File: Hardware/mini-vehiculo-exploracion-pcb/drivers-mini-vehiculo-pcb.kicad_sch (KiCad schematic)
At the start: 25 parts, among them J1 Conn_01x08_Pin_drv, J2 Conn_01x02_Pin, J3 Conn_01x02_Motor1, J4 Conn_01x02_Motor2, J5 Conn_01x02_Servo, U3 DRV8873HPWPRQ1, U4 DRV8873HPWPRQ1

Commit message: updated pcb drv
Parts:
- removed J5: Conn_01x02_Servo, symbol Connector:Conn_01x02_Pin
- added J3: Conn_01x03_Pin, symbol Connector:Conn_01x03_Pin
- C1: renamed from C9; value 1000u -> 180u; footprint (none) -> EMZR160ARA221MF61G:CAPAE660X610N
- C7: renamed from C10; value 1000u -> 180u; footprint (none) -> EMZR160ARA221MF61G:CAPAE660X610N
- J1: footprint (none) -> JST_Connectors:JST_8PIN
- renumbered C12 to C10, C4 to C11, C13 to C12, C1 to C2, C6 to C3, C7 to C4, C3 to C5, C8 to C6, C2 to C8, C11 to C9, J3 to J4, J4 to J5, R2 to R1, R5 to R2, R1 to R3, R3 to R4, R6 to R5, R4 to R6, U3 to U1, U4 to U2
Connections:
- net +5V: now also J3.1 (Pin_1)
- net GND: now also J3.3 (Pin_3)
- net CTRL_SERVO renamed SERVO_CRL
- net SERVO_CRL: now also J3.2 (Pin_2)
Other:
- added sheet Battery Sensor (battery_sensor.kicad_sch)
- note added: "IO39"
- note added: "TO SERVOMOTOR"
- note removed: "POWER SERVOMOTOR"

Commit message: cambios
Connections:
- no-connect marks 2 -> 4
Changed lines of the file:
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@@
 	)
 	(junction
+		(at 74.93 39.37)
+		(diameter 0)
+		(color 0 0 0 0)
+	)
+	(junction
 		(at 184.15 45.72)
 		(diameter 0)
@@
 	)
 	(no_connect
+		(at 74.93 102.87)
+	)
+	(no_connect
 		(at 110.49 97.79)
 	)
@@
 		(at 222.25 99.06)
 	)
+	(no_connect
+		(at 186.69 104.14)
+	)
 	(wire
 		(pts
@@
 					(unit 1)
 				)
+			)
+		)
+	)
+	(symbol
+		(lib_id "power:PWR_FLAG")
+		(at 74.93 39.37 270)
+		(unit 1)
+		(exclude_from_sim no)
+		(in_bom yes)
+		(on_board yes)
+		(dnp no)
+		(fields_autoplaced yes)
+		(property "Reference" "#FLG03"
+			(at 76.835 39.37 0)
+			(effects
+				(font
+					(size 1.27 1.27)
+				)
+				(hide yes)
+			)
+		)
+		(property "Value" "PWR_FLAG"
+			(at 78.74 39.3699 90)
+			(effects
+				(font
+					(size 1.27 1.27)
+				)
+				(justify left)
+			)
+		)
+		(property "Footprint" ""
+			(at 74.93 39.37 0)
+			(effects
+				(font
+					(size 1.27 1.27)
+				)
+				(hide yes)
+			)
+		)
+		(property "Datasheet" "~"
+			(at 74.93 39.37 0)
+			(effects
+				(font
+					(size 1.27 1.27)
+				)
+				(hide yes)
+			)
+		)
+		(property "Description" "Special symbol for telling ERC where power comes from"
+			(at 74.93 39.37 0)
+			(effects
+				(font
+					(size 1.27 1.27)
+				)
+				(hide yes)
+			)
+		)
+		(pin "1"
+		)
+		(instances
+			(project ""
+				(path "/7776e3ee-622a-4a3e-a213-279f6f5df2cb"
+					(reference "#FLG03")
+					(unit 1)
+				)

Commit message: changes etc
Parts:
- C10, C11, C2, C3, C4, C5, C8, C9: footprint capacitores_driver:CAPC2012X88N -> Capacitor_SMD:C_0805_2012Metric_Pad1.18x1.45mm_HandSolder
- C12, C6: footprint capacitores_driver:CAPC2012X140N -> Capacitor_SMD:C_0805_2012Metric_Pad1.18x1.45mm_HandSolder
- J1: footprint JST_Connectors:JST_8PIN -> Connector_PinSocket_2.54mm:PinSocket_1x08_P2.54mm_Vertical
- J2, J4, J5: footprint (none) -> Connector_PinSocket_2.54mm:PinSocket_1x02_P2.54mm_Vertical
- J3: footprint (none) -> Connector_PinSocket_2.54mm:PinSocket_1x03_P2.54mm_Vertical
- U1, U2: footprint DRV8873HPWPRQ1:DRV8873HPWPRQ1 -> DRV8873HPWPRQ1:SOP65P640X120-25N

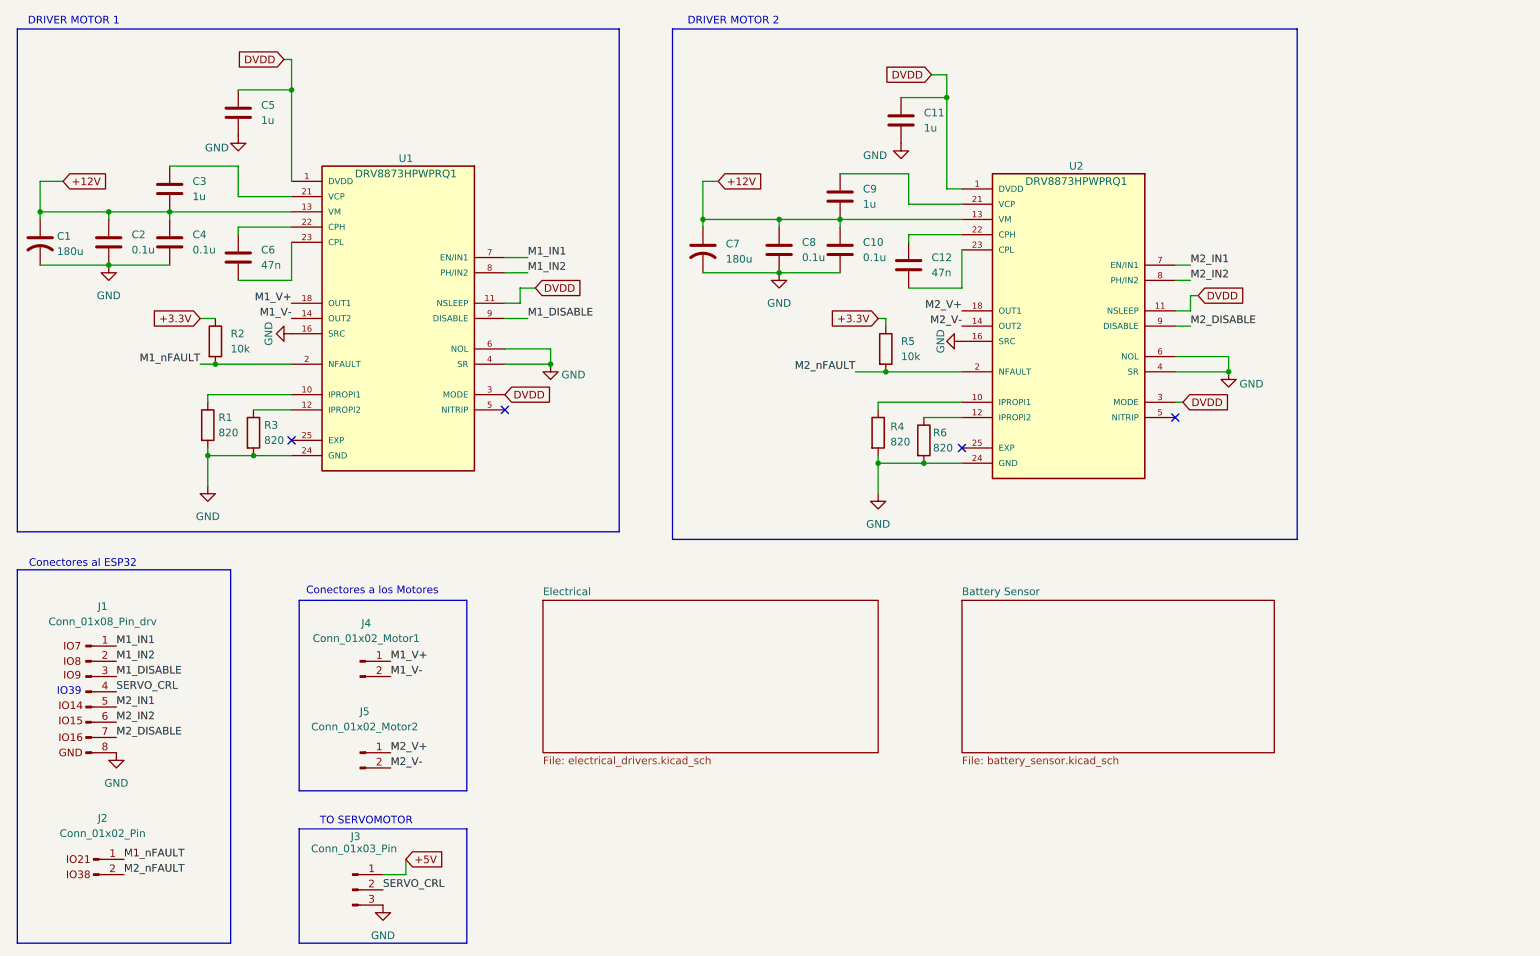
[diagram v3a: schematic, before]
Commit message: updated sockets drv
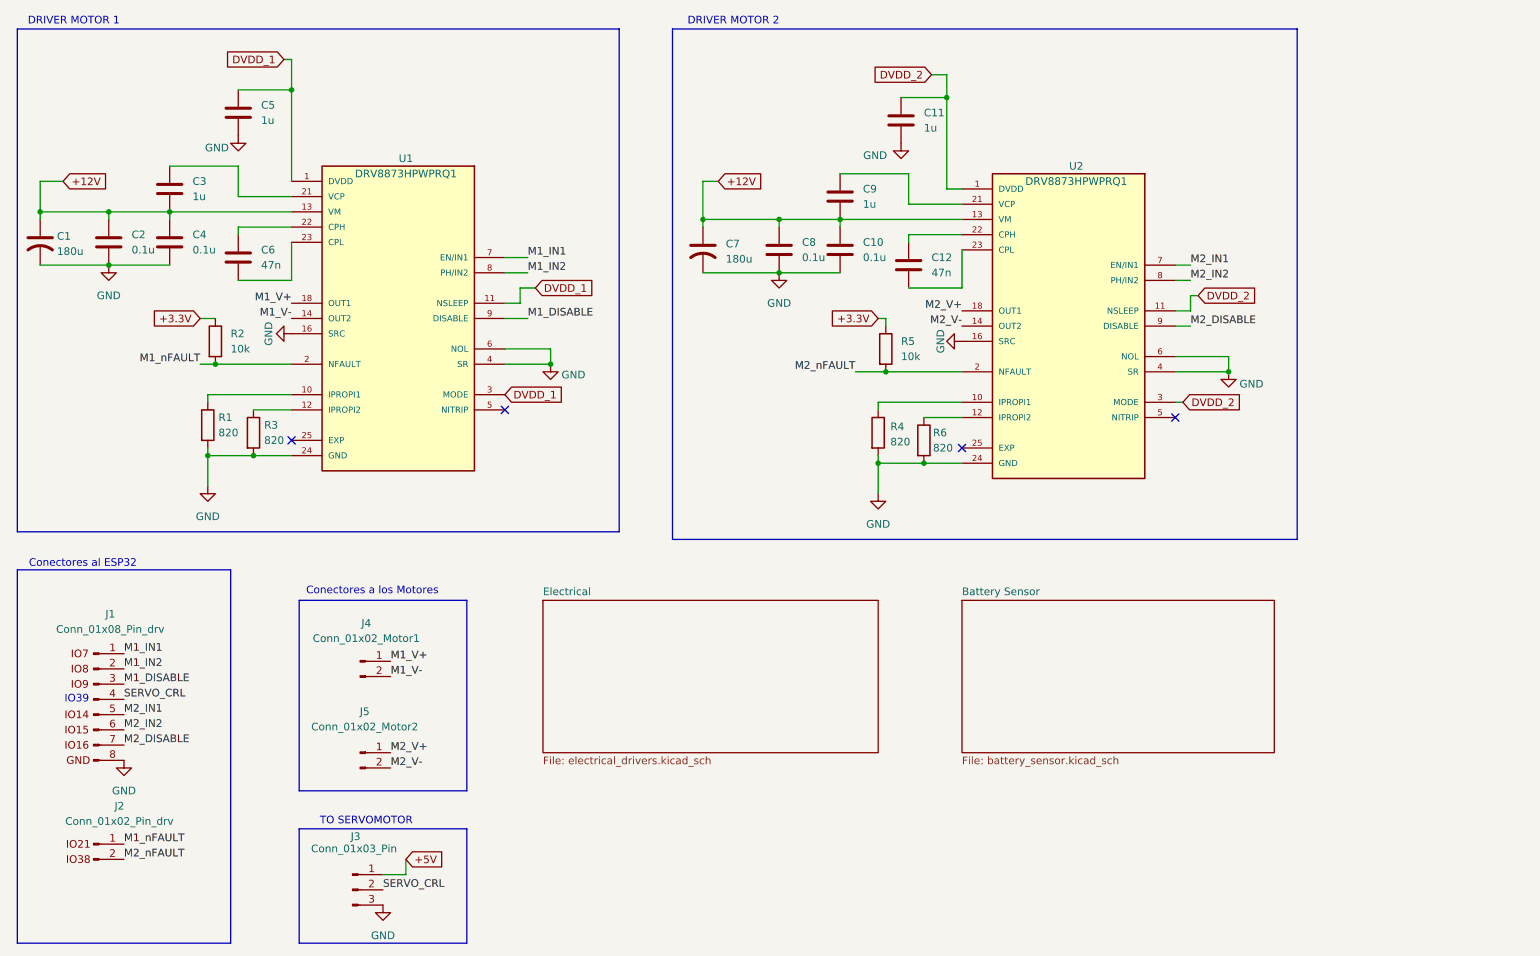
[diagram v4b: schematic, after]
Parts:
- removed J2: Conn_01x02_Pin, Connector_PinSocket_2.54mm:PinSocket_1x02_P2.54mm_Vertical, symbol Connector:Conn_01x02_Pin
- added J2: Conn_01x02_Pin_drv, symbol ConectorDriverESP:Conn_01x02_Pin_drv
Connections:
- net M1_nFAULT: now also J2.1 (Pin_1)
- net M2_nFAULT: now also J2.2 (Pin_2)
- net DVDD renamed DVDD_1
- net DVDD_1: no longer C11.1, U2.1 (DVDD), U2.11 (NSLEEP), U2.3 (MODE)
- new net DVDD_2: C11.1, U2.1 (DVDD), U2.11 (NSLEEP), U2.3 (MODE)
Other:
- moved on the sheet: J1
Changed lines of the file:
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@@
 	(text "IO39"
 		(exclude_from_sim no)
-		(at 37.846 144.78 0)
+		(at 39.116 146.05 0)
 		(effects
 			(font
@@
 	)
 	(label "M2_IN2"
-		(at 45.72 149.86 0)
+		(at 46.99 151.13 0)
 		(effects
 			(font
@@
 	)
 	(label "M1_IN2"
-		(at 45.72 139.7 0)
+		(at 46.99 140.97 0)
 		(effects
 			(font
@@
 	)
 	(label "M2_IN1"
-		(at 45.72 147.32 0)
+		(at 46.99 148.59 0)
 		(effects
 			(font
@@
 	)
 	(label "M1_IN1"
-		(at 45.72 137.16 0)
+		(at 46.99 138.43 0)
 		(effects
 			(font
@@
 	)
 	(label "SERVO_CRL"
-		(at 45.72 144.78 0)
+		(at 46.99 146.05 0)
 		(effects
 			(font
@@
 	)
 	(label "M1_DISABLE"
-		(at 45.72 142.24 0)
+		(at 46.99 143.51 0)
 		(effects
 			(font
@@
 	)
 	(label "M1_nFAULT"
-		(at 46.99 172.72 0)
+		(at 46.99 170.18 0)
 		(effects
 			(font
@@
 	)
 	(label "M2_DISABLE"
-		(at 45.72 152.4 0)
+		(at 46.99 153.67 0)
 		(effects
 			(font
@@
 	)
 	(label "M2_nFAULT"
-		(at 46.99 175.26 0)
+		(at 46.99 172.72 0)
 		(effects
 			(font
@@
 		)
 	)
-	(global_label "DVDD"
+	(global_label "DVDD_1"
 		(shape input)
 		(at 115.57 77.47 0)
@@
 		)
 		(property "Intersheetrefs" "${INTERSHEET_REFS}"
-			(at 123.4538 77.47 0)
+			(at 125.6309 77.47 0)
 			(effects
 				(font
@@
 		)
 	)
-	(global_label "DVDD"
+	(global_label "DVDD_2"
 		(shape input)
 		(at 226.06 78.74 0)
@@
 		)
 		(property "Intersheetrefs" "${INTERSHEET_REFS}"
-			(at 233.9438 78.74 0)
+			(at 236.1209 78.74 0)
 			(effects
 				(font
@@
 		)
 	)
-	(global_label "DVDD"
+	(global_label "DVDD_2"
 		(shape input)
 		(at 181.61 41.91 180)
@@
 		)
 		(property "Intersheetrefs" "${INTERSHEET_REFS}"
-			(at 173.7262 41.91 0)
+			(at 171.5491 41.91 0)
 			(effects
 				(font
@@
 		)
 	)
-	(global_label "DVDD"
+	(global_label "DVDD_1"
 		(shape input)
 		(at 73.66 39.37 180)
@@
 		)
 		(property "Intersheetrefs" "${INTERSHEET_REFS}"
-			(at 65.7762 39.37 0)
+			(at 63.5991 39.37 0)
 			(effects
 				(font
@@
 		)
 	)
-	(global_label "DVDD"
+	(global_label "DVDD_1"
 		(shape input)
 		(at 110.49 95.25 0)
@@
 		)
 		(property "Intersheetrefs" "${INTERSHEET_REFS}"
-			(at 118.3738 95.25 0)
+			(at 120.5509 95.25 0)
 			(effects
 				(font
@@
 		)
 	)
-	(global_label "DVDD"
+	(global_label "DVDD_2"
 		(shape input)
 		(at 223.52 96.52 0)
@@
 		)
 		(property "Intersheetrefs" "${INTERSHEET_REFS}"
-			(at 231.4038 96.52 0)
+			(at 233.5809 96.52 0)
 			(effects
 				(font
@@
 	)
 	(symbol
+		(lib_id "ConectorDriverESP:Conn_01x02_Pin_drv")
+		(at 41.91 170.18 0)
+		(unit 1)
+		(exclude_from_sim no)
+		(in_bom yes)
+		(on_board yes)
+		(dnp no)
+		(property "Reference" "J2"
+			(at 46.228 163.83 0)
+			(effects
+				(font
+					(size 1.27 1.27)
+				)
+			)
+		)
+		(property "Value" "Conn_01x02_Pin_drv"
+			(at 46.228 166.37 0)
+			(effects
+				(font
+					(size 1.27 1.27)
+				)
+			)
+		)
+		(property "Footprint" ""
+			(at 41.91 170.18 0)
+			(effects
+				(font
+					(size 1.27 1.27)
+				)
+				(hide yes)
+			)
+		)
+		(property "Datasheet" "~"
+			(at 41.91 170.18 0)
+			(effects
+				(font
+					(size 1.27 1.27)
+				)
+				(hide yes)
+			)
+		)
+		(property "Description" "Generic connector, single row, 01x02, script generated"
+			(at 41.91 170.18 0)
+			(effects
+				(font
+					(size 1.27 1.27)
+				)
+				(hide yes)
+			)
+		)
+		(pin "1"
+		)
+		(pin "2"
+		)
+		(instances
+			(project ""
+				(path "/7776e3ee-622a-4a3e-a213-279f6f5df2cb"
+					(reference "J2")
+					(unit 1)
+				)
+			)
+		)
+	)
+	(symbol
 		(lib_id "Device:R")
 		(at 68.58 101.6 0)
@@
 	(symbol
 		(lib_id "ConectorDriverESP:Conn_01x08_Pin_drv")
-		(at 40.64 144.78 0)
+		(at 41.91 146.05 0)
 		(unit 1)
 		(exclude_from_sim no)
@@
 		(dnp no)
 		(property "Reference" "J1"
-			(at 43.434 130.556 0)
+			(at 44.704 131.826 0)
 			(effects
 				(font
@@
 		)
 		(property "Value" "Conn_01x08_Pin_drv"
-			(at 43.434 133.096 0)
+			(at 44.704 134.366 0)
 			(effects
 				(font
@@
 		)
 		(property "Footprint" "Connector_PinSocket_2.54mm:PinSocket_1x08_P2.54mm_Vertical"
-			(at 40.64 144.78 0)
+			(at 41.91 146.05 0)
 			(effects
 				(font
@@
 		)
 		(property "Datasheet" "~"
-			(at 40.64 144.78 0)
+			(at 41.91 146.05 0)
 			(effects
 				(font
@@
 		)
 		(property "Description" "Generic connector, single row, 01x08, script generated"
-			(at 39.624 128.27 0)
+			(at 40.894 129.54 0)
 			(effects
 				(font
@@
 	(symbol
 		(lib_id "power:GND")
-		(at 45.72 154.94 0)
+		(at 46.99 156.21 0)
 		(unit 1)
 		(exclude_from_sim no)
@@
 		(fields_autoplaced yes)
 		(property "Reference" "#PWR02"
-			(at 45.72 161.29 0)
+			(at 46.99 162.56 0)
 			(effects
 				(font
@@
 		)
 		(property "Value" "GND"
-			(at 45.72 160.02 0)
+			(at 46.99 161.29 0)
 			(effects
 				(font
@@
 		)
 		(property "Footprint" ""
-			(at 45.72 154.94 0)
+			(at 46.99 156.21 0)
 			(effects
 				(font
@@
 		)
 		(property "Datasheet" ""
-			(at 45.72 154.94 0)
+			(at 46.99 156.21 0)
 			(effects
 				(font
@@
 		)
 		(property "Description" "Power symbol creates a global label with name \"GND\" , ground"
-			(at 45.72 154.94 0)
+			(at 46.99 156.21 0)
 			(effects
 				(font
@@
 					(unit 1)
 				)
-			)
-		)
-	)
-	(symbol
-		(lib_id "Connector:Conn_01x02_Pin")
-		(at 41.91 172.72 0)
-		(unit 1)
-		(exclude_from_sim no)
-		(in_bom yes)
-		(on_board yes)
-		(dnp no)
-		(property "Reference" "J2"
-			(at 43.434 165.862 0)
-			(effects
-				(font
-					(size 1.27 1.27)
-				)
-			)
-		)
-		(property "Value" "Conn_01x02_Pin"
-			(at 43.434 168.402 0)
-			(effects
-				(font
-					(size 1.27 1.27)
-				)
-			)
-		)
-		(property "Footprint" "Connector_PinSocket_2.54mm:PinSocket_1x02_P2.54mm_Vertical"
-			(at 41.91 172.72 0)
-			(effects
-				(font
-					(size 1.27 1.27)
-				)
-				(hide yes)
-			)
-		)
-		(property "Datasheet" "~"
-			(at 41.91 172.72 0)
-			(effects
-				(font
-					(size 1.27 1.27)
-				)
-				(hide yes)
-			)
-		)
-		(property "Description" "Generic connector, single row, 01x02, script generated"
-			(at 41.91 172.72 0)
-			(effects
-				(font
-					(size 1.27 1.27)
-				)
-				(hide yes)
-			)
-		)
-		(pin "1"
-		)
-		(pin "2"
-		)
-		(instances
-			(project ""
-				(path "/7776e3ee-622a-4a3e-a213-279f6f5df2cb"
-					(reference "J2")
-					(unit 1)
-				)

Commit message: Add netclassses, mounting holes and terminal block
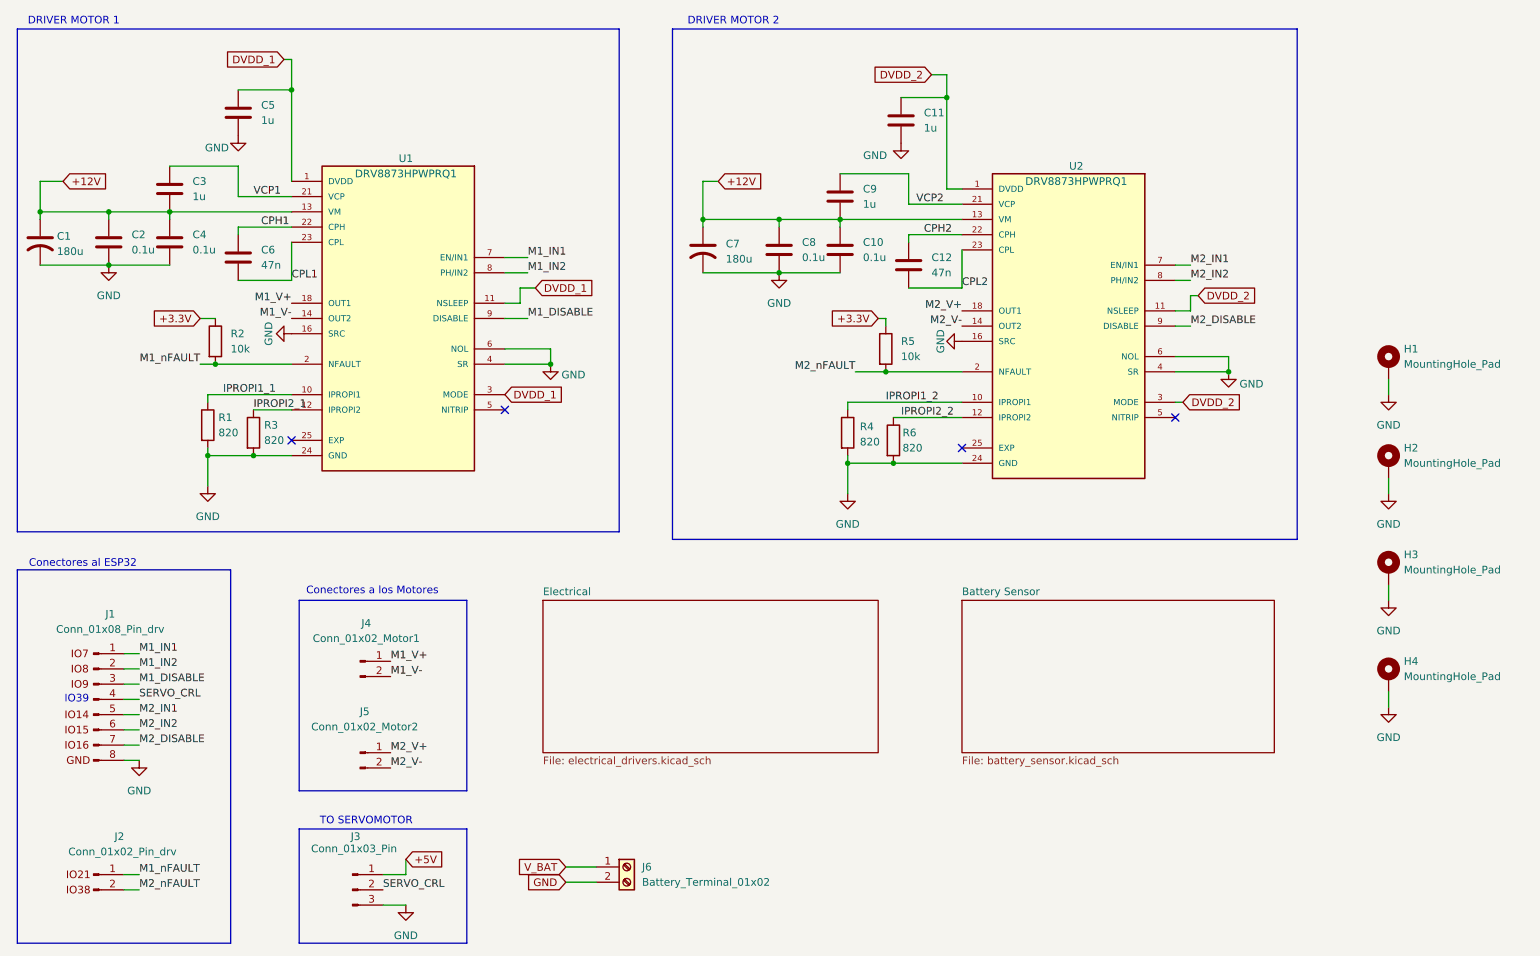
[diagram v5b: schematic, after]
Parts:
- added H1, H2, H3, H4: MountingHole_Pad, MountingHole:MountingHole_3.2mm_M3_Pad_Via, symbol Mechanical:MountingHole_Pad
- added J6: Battery_Terminal_01x02, TerminalBlock_Phoenix:TerminalBlock_Phoenix_MPT-0,5-2-2.54_1x02_P2.54mm_Horizontal, symbol Connector:Screw_Terminal_01x02
- J2: footprint (none) -> Connector_PinSocket_2.54mm:PinSocket_1x02_P2.54mm_Vertical
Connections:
- net GND: now also H1.1, H2.1, H3.1, H4.1, J6.2 (Pin_2)
- net IPROPI1_1: now reaches R1.1, U1.10 (IPROPI1)
- net VCP2: now reaches C9.1, U2.21 (VCP)
- net IPROPI2_2: now reaches R6.1, U2.12 (IPROPI2)
- net IPROPI2_1: now reaches R3.1, U1.12 (IPROPI2)
- net IPROPI1_2: now reaches R4.1, U2.10 (IPROPI1)
- net VCP1: now reaches C3.1, U1.21 (VCP)
- net CPH1: now reaches C6.1, U1.22 (CPH)
- net CPL1: now reaches C6.2, U1.23 (CPL)
- net CPH2: now reaches C12.1, U2.22 (CPH)
- net CPL2: now reaches C12.2, U2.23 (CPL)
- new net V_BAT: J6.1 (Pin_1)
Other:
- moved on the sheet: J2, R4, R6

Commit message: Revert "cambios"
This reverts commit 18d6c077649d06db3e4be51193d20dbced0bef3d, reversing
changes made to f53350afebab44693d0a4c4c217b64a1fc0c425b.
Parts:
- removed H1, H2, H3, H4: MountingHole_Pad, MountingHole:MountingHole_3.2mm_M3_Pad_Via, symbol Mechanical:MountingHole_Pad
- removed J6: Battery_Terminal_01x02, TerminalBlock_Phoenix:TerminalBlock_Phoenix_MPT-0,5-2-2.54_1x02_P2.54mm_Horizontal, symbol Connector:Screw_Terminal_01x02
- J2: footprint Connector_PinSocket_2.54mm:PinSocket_1x02_P2.54mm_Vertical -> (none)
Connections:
- net CPH1: no longer names the net of C6.1, U1.22 (CPH)
- net CPH2: no longer names the net of C12.1, U2.22 (CPH)
- net CPL1: no longer names the net of C6.2, U1.23 (CPL)
- net CPL2: no longer names the net of C12.2, U2.23 (CPL)
- net IPROPI1_1: no longer names the net of R1.1, U1.10 (IPROPI1)
- net IPROPI1_2: no longer names the net of R4.1, U2.10 (IPROPI1)
- net IPROPI2_1: no longer names the net of R3.1, U1.12 (IPROPI2)
- net IPROPI2_2: no longer names the net of R6.1, U2.12 (IPROPI2)
- net VCP1: no longer names the net of C3.1, U1.21 (VCP)
- net VCP2: no longer names the net of C9.1, U2.21 (VCP)
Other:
- moved on the sheet: J2, R4, R6
